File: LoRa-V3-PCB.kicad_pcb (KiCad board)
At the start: 2 copper layers, 62 x 50 mm, 87 parts, among them IC1 114993121, IC10 BR24G1MFVT-5AE2, IC11 BR24G1MFVT-5AE2, IC13 MCP73123T-22SI/MF, IC2 CP2102N-Axx-xQFN24, IC3 USBLC6-2P6, IC4 BQ25504RGTR, IC5 BME680, IC6 SHT40-BD1B-R2, IC7 TSL25911FN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

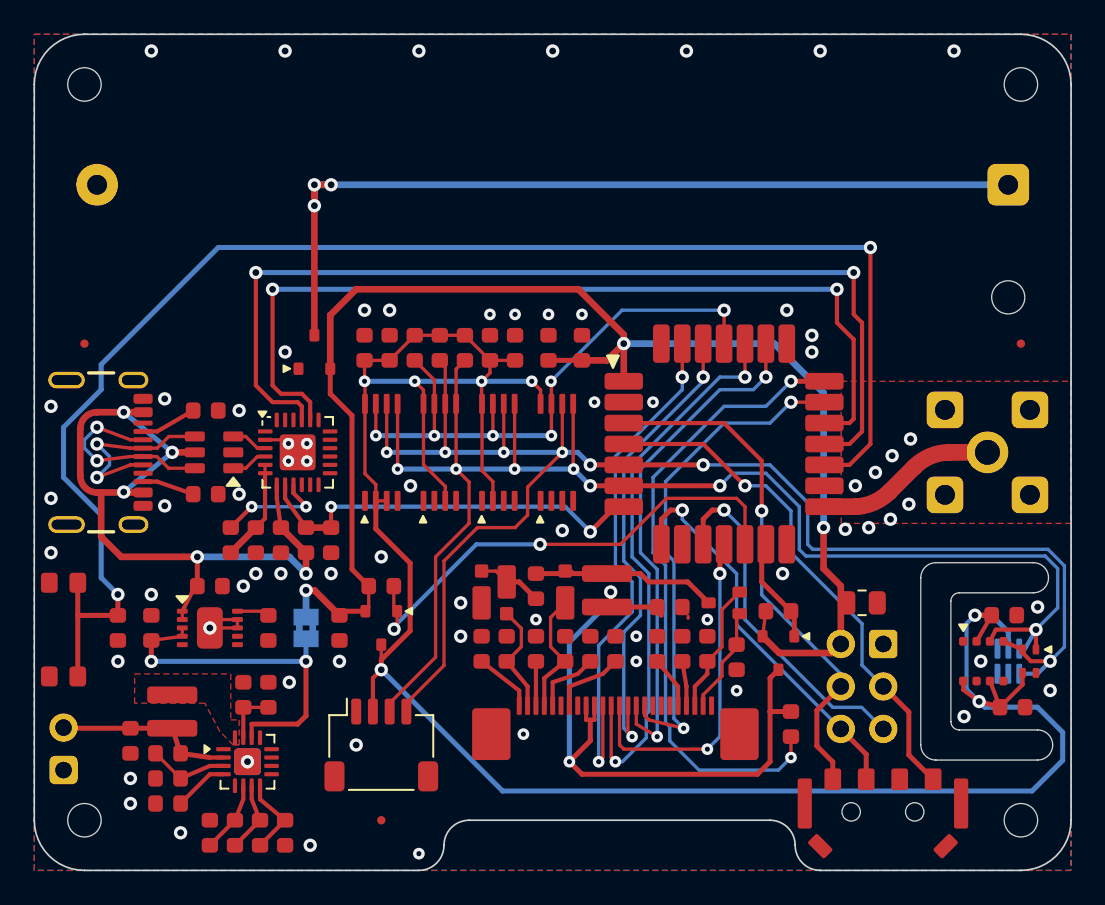
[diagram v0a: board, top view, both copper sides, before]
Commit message: reworked for 0805 capacitors
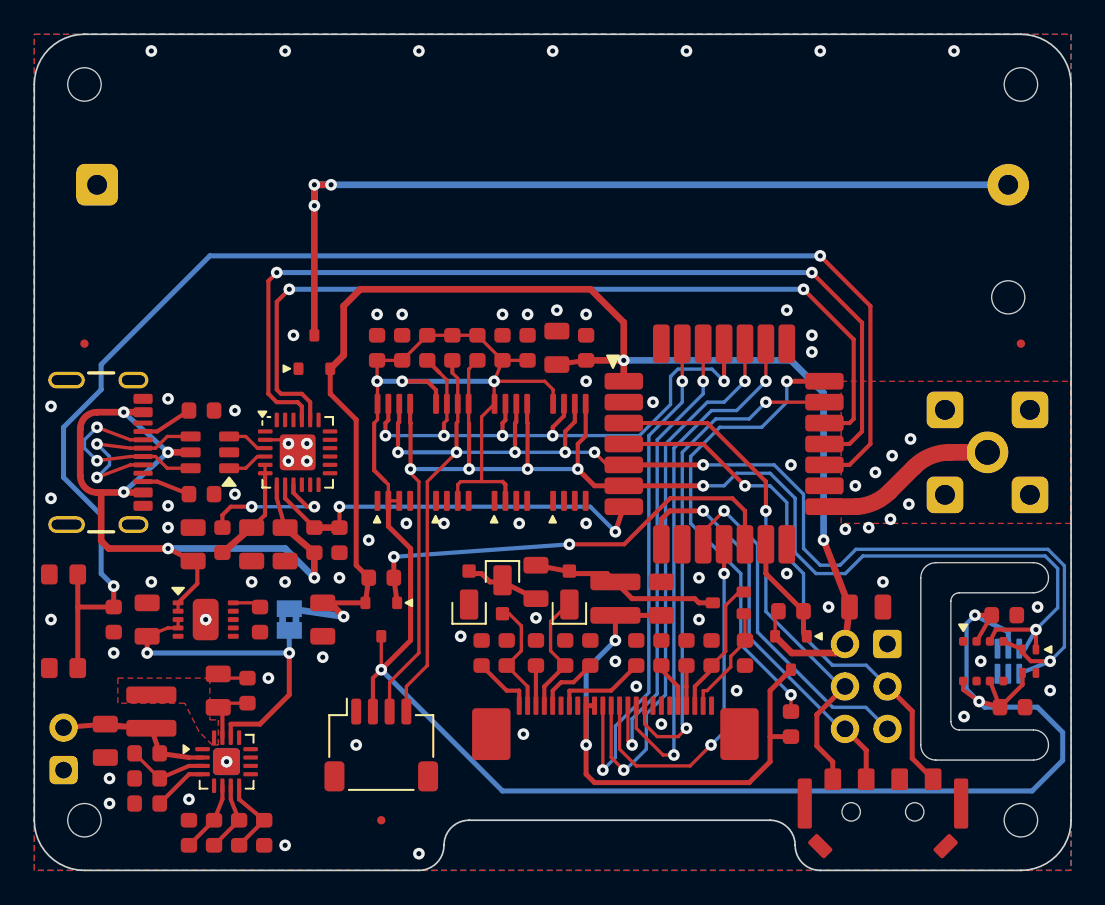
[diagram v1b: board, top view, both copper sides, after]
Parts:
- C1, C2, C3, C4, C5, C6, C7, C8: value CGA3E2X7R1E104K080AA -> 100nF
- C10: value C1608X7S1A475K080AC -> 10uF; footprint 1projectLibrary:C_0603_nominal -> 1projectLibrary:C_0805
- C11, C12, C13, C14, C15, C16: value C1608X7S1A475K080AC -> 4.7uF; footprint 1projectLibrary:C_0603_nominal -> 1projectLibrary:C_0805
- C18: value C1608X7S1A475K080AC -> 10uF; footprint Resistor_SMD:R_0805_2012Metric -> 1projectLibrary:C_0805
- C20: value ~ -> 4.7uF; footprint 1projectLibrary:C_0603_nominal -> 1projectLibrary:C_0805
- C22, C25: value C0603C106M8PACTU -> 10uF; footprint 1projectLibrary:C_0603_nominal -> 1projectLibrary:C_0805
- C30, C31, C32, C33, C34, C35, C36, C37: value CGA3E1X7R1E105K080AC -> 1uF
- CONN2: value 1015 -> LiFePO4 battery
- L1: value VLS3010CX-470M-1 -> 47uH
- L2: value VLS3010CX-220M-1 -> 22 uH
- R10, R5, R6, R7, R8, R9: value CR0603-FX-5101ELF -> 5K1
- R11, R21: value CR0603-FX-7501ELF -> 5M36
- R12: value CR0603-FX-1002ELF -> 10K
- R13: value CR0603-FX-2212ELF -> 22K1
- R14, R20: value CR0603-FX-3742ELF -> 4M75
- R15: value CR0603-FX-4752ELF -> 47K5
- R17, R18: value CR0603-FX-1004ELF -> 330K
- R19: value CR0603-FX-2203ELF -> 8M45
- R2: value CR0603-FX-2203ELF -> 1M69
- R23: value CR0603-FX-2203ELF -> 330
- R3: value CR0603-FX-1001ELF -> 1K
- moved C11 2.69 mm to (123.5, 102.5), turned to 90 degrees
- moved C16 1.52 mm to (125.0, 111.2)
- moved C20 1.50 mm to (118.2, 114.2)
- moved C17 1.27 mm to (126.8, 111.2)
- moved C34 1.27 mm to (150.0, 109.0)
- moved C9 1.25 mm to (120.8, 118.0)
- moved IC4 1.25 mm to (125.5, 115.5)
- moved L2 1.25 mm to (121.0, 112.5)
- moved R11 1.25 mm to (127.8, 119.8)
- moved R14 1.25 mm to (126.2, 119.8)
- moved R19 1.25 mm to (120.8, 116.5)
- moved R2 1.25 mm to (120.8, 115.0)
- moved R20 1.25 mm to (124.8, 119.8)
- moved R21 1.25 mm to (123.2, 119.8)
- moved C25 1.12 mm to (131.2, 107.0)
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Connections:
- C18 pad 1: GND -> +3.3V
- C18 pad 2: +3.3V -> GND
- CONN2 pad 1: VBAT -> GND
- CONN2 pad 2: GND -> VBAT
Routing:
- net VDD-Display-Charge: track 38.1 -> 28.1 mm
- net VDD-Display: track 40.6 -> 34.8 mm
- net ~{MCU-RESET}: track 90.4 -> 86.1 mm
- net I2C2-SCL: track 92.9 -> 88.9 mm
- net UART2-RX: track 59.1 -> 56.1 mm
- net I2C2-SDA: track 91.3 -> 88.9 mm, vias 7 -> 6
- net +5V: track 46.2 -> 48.6 mm
- net GND: track 5.33 -> 3.05 mm, vias 70 -> 76
- net ~{Enable-3.3V-Switched-1}: track 29.5 -> 27.2 mm
- net UART2-TX: track 53.0 -> 51.0 mm
- net RST: track 6.65 -> 8.52 mm
- net SWCLK: track 31.2 -> 32.6 mm
- net ~{DISPLAY-RESET}: track 30.8 -> 32.0 mm
- net VDD: track 4.35 -> 5.52 mm
- net ~{DISPLAY-CS}: track 20.3 -> 21.3 mm
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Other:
- outline, holes or cut-outs redrawn

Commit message: fix missing 3D models
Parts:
- IC7: footprint 1GlobalFootprintsLibrary:TSL2591 -> 1projectLibrary:TSL2591
- SW2: footprint 1GlobalFootprintsLibrary:SLLB510100 -> 1projectLibrary:SLLB510100
- moved C3 0.89 mm to (172.0, 105.9)
- moved C4 0.89 mm to (172.5, 111.4)
- moved IC5 0.89 mm to (170.8, 108.6)
- moved IC6 0.89 mm to (173.5, 108.6)
- moved IC7 0.89 mm to (172.2, 108.6)
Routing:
- net VDD-SENSORS-EEPROM: track 134.5 -> 135.4 mm
- net I2C2-SCL: track 88.9 -> 89.4 mm
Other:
- outline, holes or cut-outs redrawn

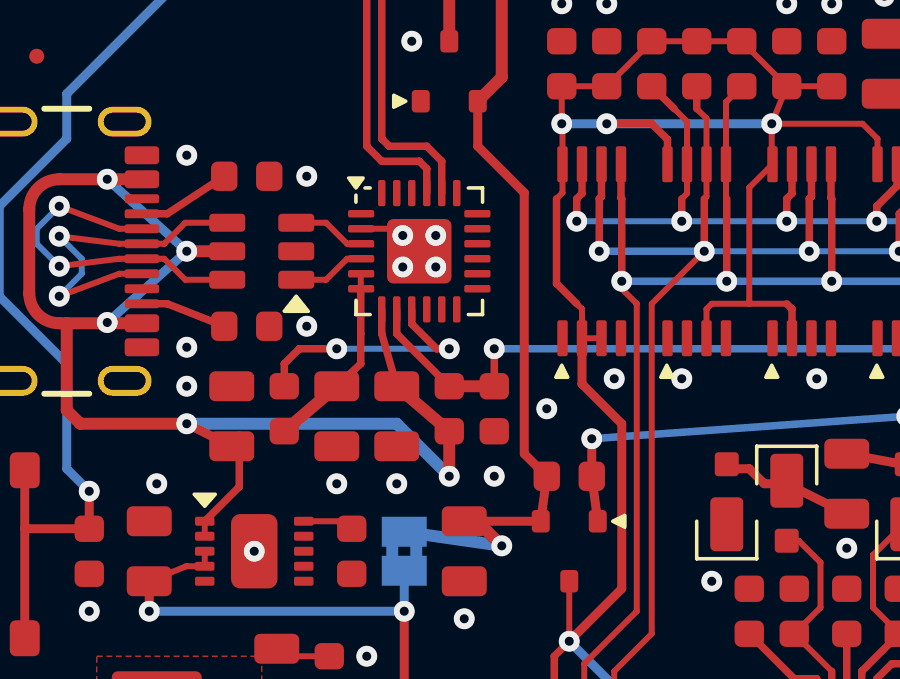
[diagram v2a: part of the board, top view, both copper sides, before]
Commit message: fix footprint for CP2102N
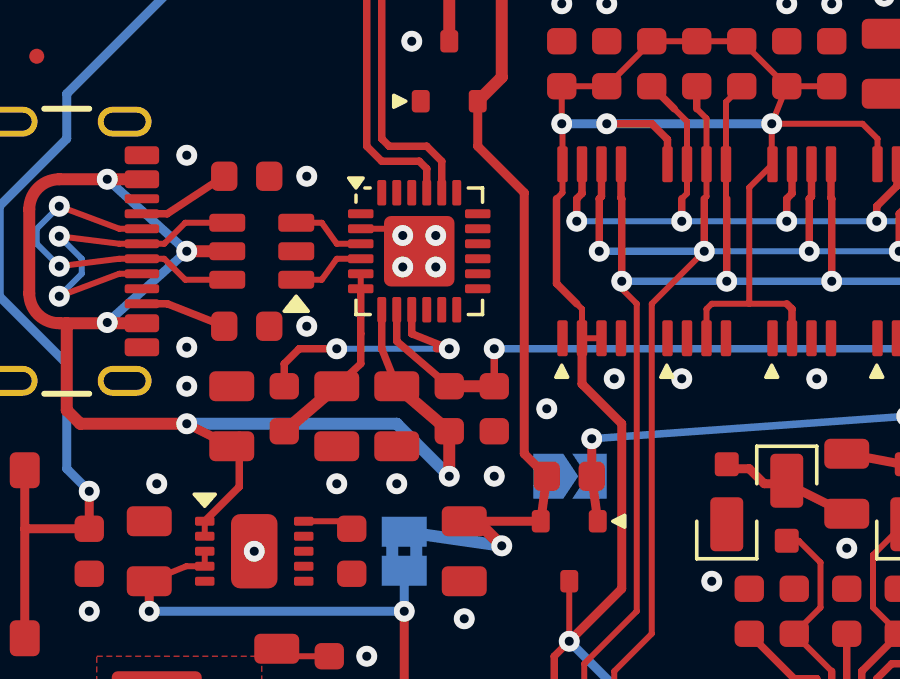
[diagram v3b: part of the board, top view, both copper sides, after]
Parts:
- added JP2: NA, 1projectLibrary:SolderJumper-2_P1.3mm_Open_TrianglePad1.0x1.5mm, B.Cu at (134.8, 104.5)
- IC2: footprint 1projectLibrary:QFN-24-1EP_4x4mm_P0.5mm_EP2.15x2.15mm-epeas -> 1projectLibrary:QFN24-CP2102N
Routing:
- net ~{Enable-3.3V-Switched-1}: track 27.2 -> 28.5 mm
- net RST: track 8.52 -> 9.03 mm

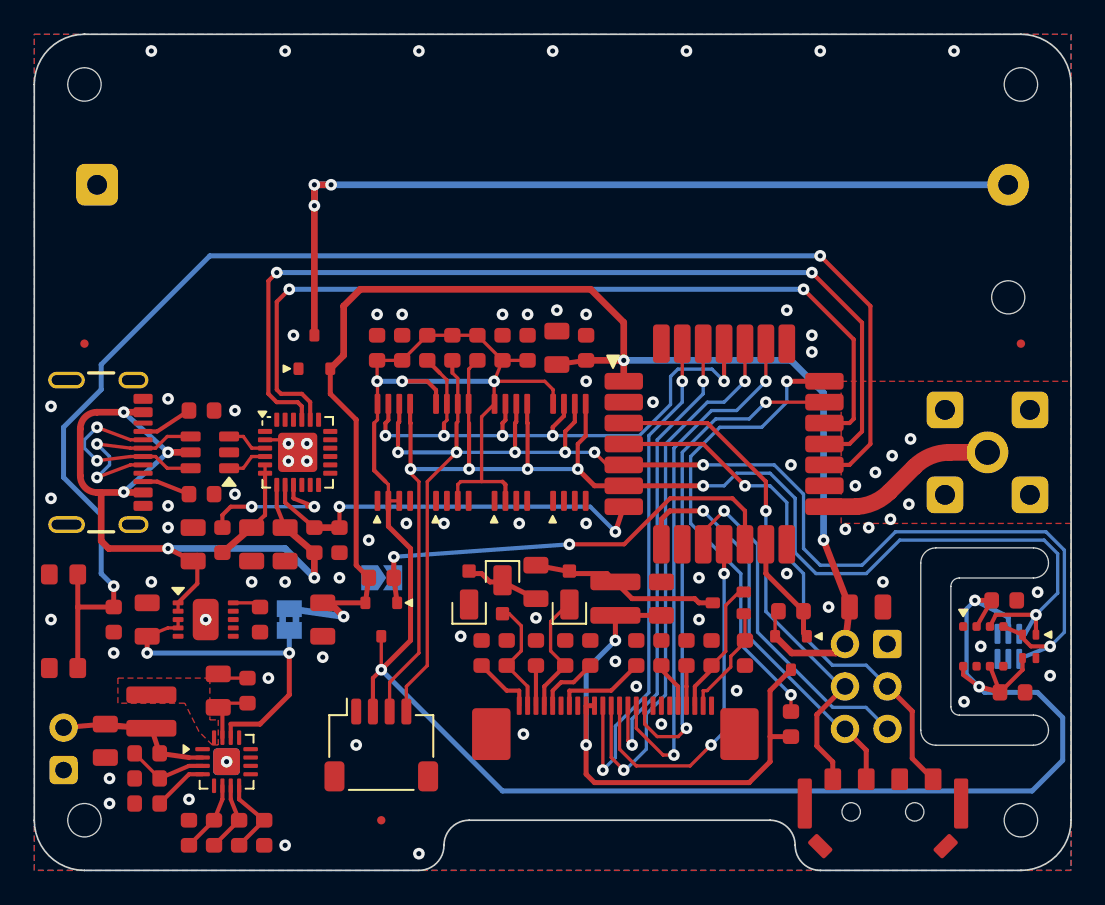
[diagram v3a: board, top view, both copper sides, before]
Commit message: add permanent vdd for sensors with solder bridge
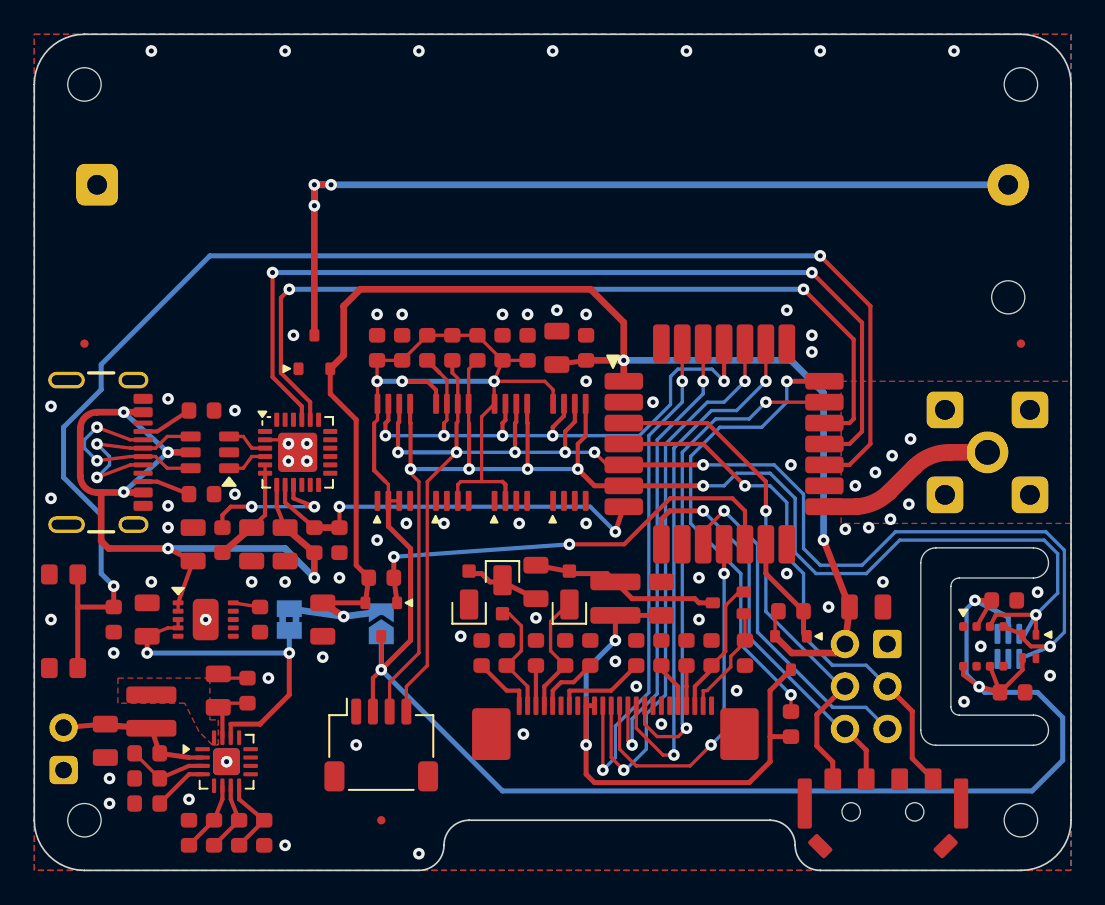
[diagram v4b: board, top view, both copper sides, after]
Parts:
- moved JP2 2.75 mm to (134.8, 107.2), turned to 90 degrees
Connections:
- JP2 pad 1: GND -> VDD-SENSORS-EEPROM
- JP2 pad 2: ~{Enable-3.3V-Switched-1} -> +3.3V
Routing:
- net +3.3V: track 86.5 -> 88.6 mm
- net VDD-SENSORS-EEPROM: track 135.4 -> 137.5 mm
- net ~{Enable-3.3V-Switched-1}: track 28.5 -> 27.2 mm
- net UART2-TX: track 51.0 -> 50.1 mm
- net UART2-RX: track 56.1 -> 55.3 mm
- net +5V: track 48.6 -> 48.0 mm
